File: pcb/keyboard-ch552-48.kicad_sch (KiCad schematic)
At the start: 112 parts, among them J1 USB_C_Receptacle_USB2.0, SW1 SW_SPST, SW2 SW_SPST, U1 CH552T

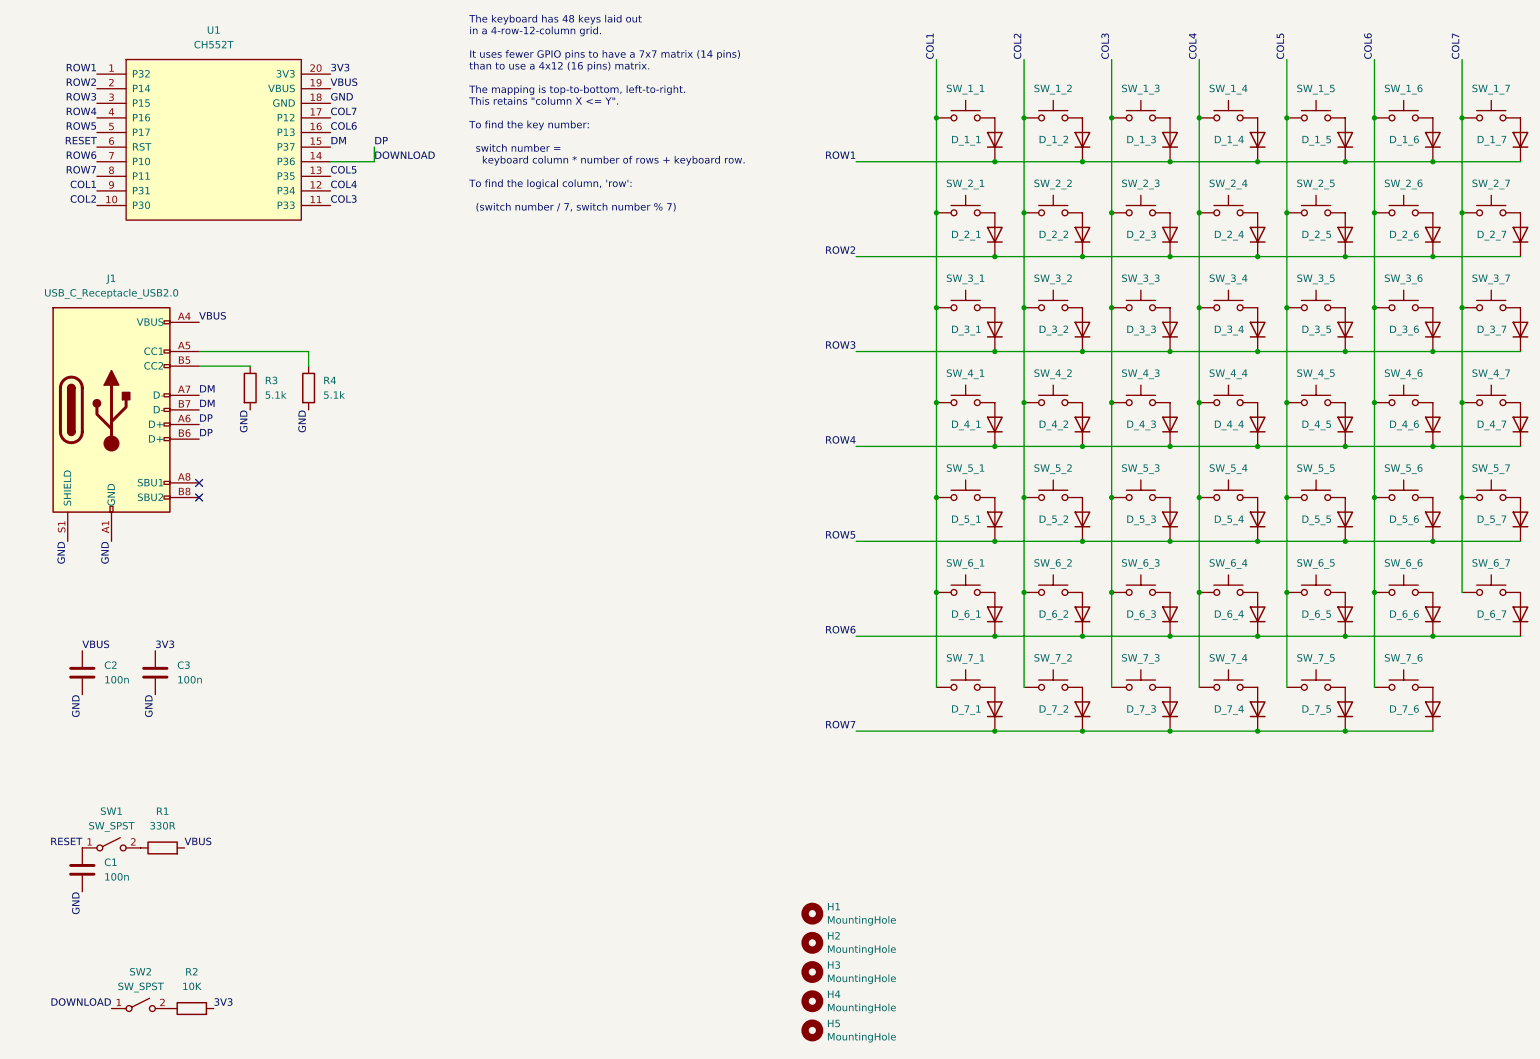
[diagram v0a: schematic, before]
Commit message: pcb: break out SPI pins for ISP flash on CH552-48
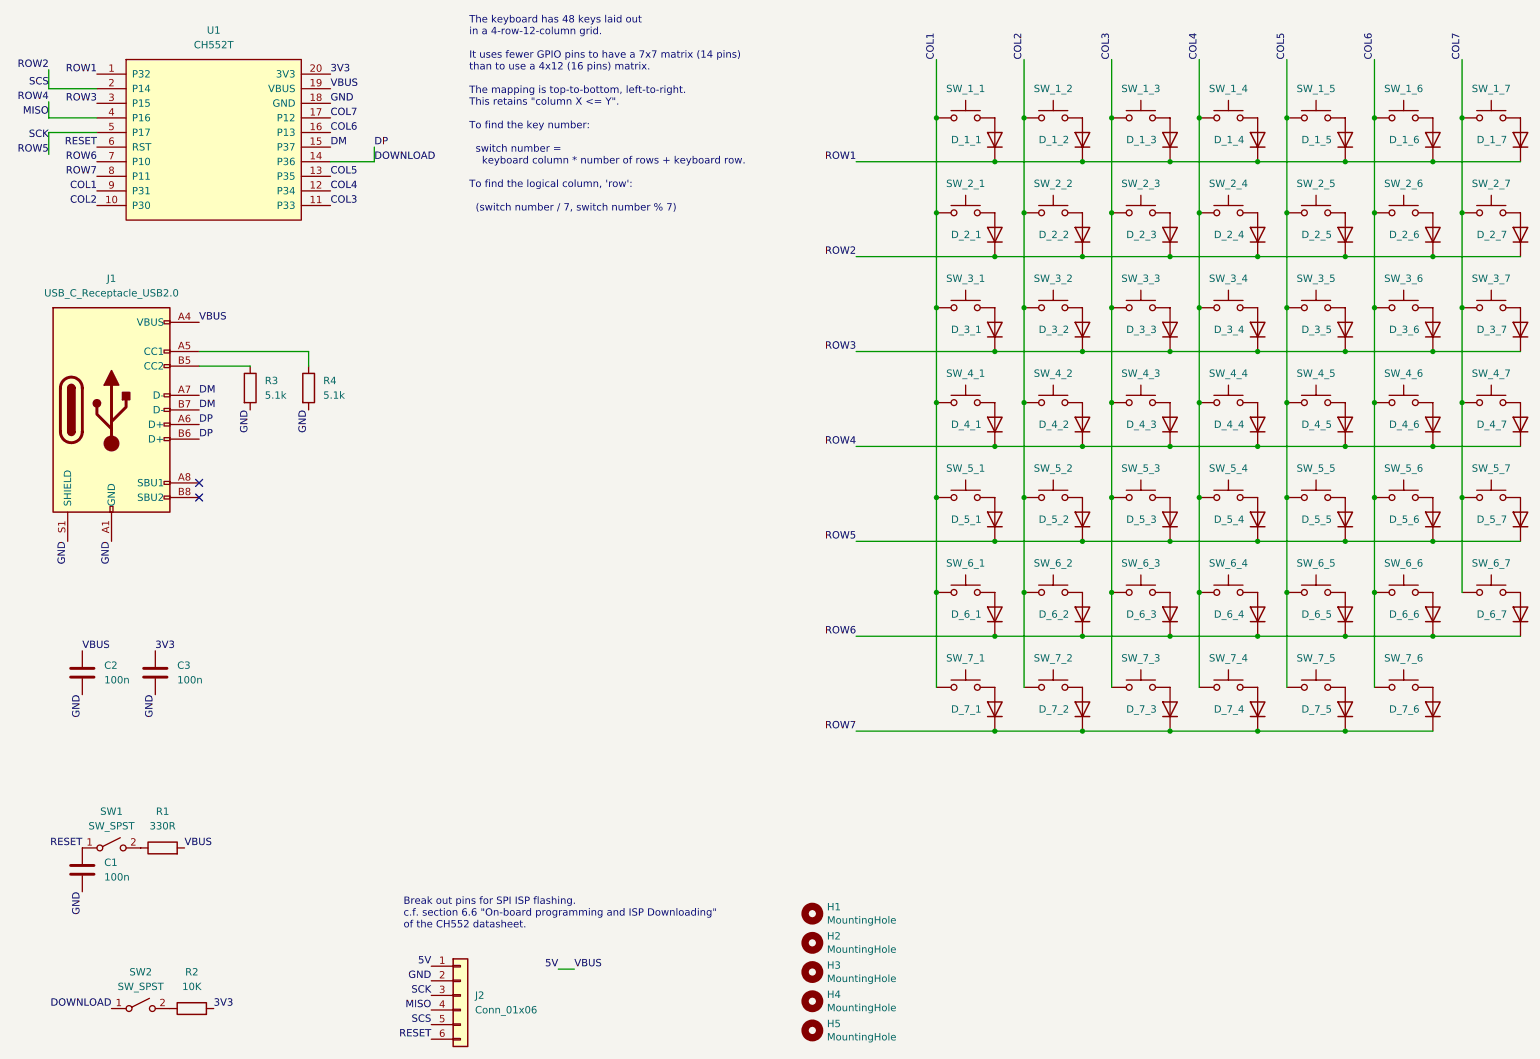
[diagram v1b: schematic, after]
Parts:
- added J2: Conn_01x06, symbol Connector_Generic:Conn_01x06
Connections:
- net GND: now also J2.2 (Pin_2)
- net RESET: now also J2.6 (Pin_6)
- net ROW2: now also J2.5 (Pin_5)
- net ROW5: now also J2.3 (Pin_3)
- net ROW4 renamed MISO
- net MISO: now also J2.4 (Pin_4)
- net VBUS renamed 5V
- net 5V: now also J2.1 (Pin_1)
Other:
- note added: "Break out pins for SPI ISP flashing. c.f. section 6.6 "On-board programming and ISP Downloading" of the CH552 datasheet."
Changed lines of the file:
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@@
   (title_block
     (title "CH552-48")
-    (date "2023-11-10")
-    (rev "rev2023.1")
+    (date "2024-01-03")
+    (rev "rev2024.1-pre")
     (company "Richard Goulter (rgoulter)")
     (comment 1 "48-key on 7x7 logical grid.")
@@
     (stroke (width 0) (type default))
   )
+  (wire (pts (xy 112.014 179.832) (xy 114.808 179.832))
+    (stroke (width 0) (type default))
+  )
   (wire (pts (xy 187.96 138.43) (xy 163.83 138.43))
     (stroke (width 0) (type default))
@@
     (stroke (width 0) (type default))
   )
+  (wire (pts (xy 23.368 28.956) (xy 23.368 31.75))
+    (stroke (width 0) (type default))
+  )
   (wire (pts (xy 254 97.79) (xy 254 114.3))
     (stroke (width 0) (type default))
@@
     (stroke (width 0) (type default))
   )
+  (wire (pts (xy 23.368 26.67) (xy 31.75 26.67))
+    (stroke (width 0) (type default))
+  )
   (wire (pts (xy 233.68 88.9) (xy 248.92 88.9))
     (stroke (width 0) (type default))
@@
     (stroke (width 0) (type default))
   )
+  (wire (pts (xy 23.368 31.75) (xy 31.75 31.75))
+    (stroke (width 0) (type default))
+  )
   (wire (pts (xy 223.52 114.3) (xy 223.52 130.81))
     (stroke (width 0) (type default))
@@
     (stroke (width 0) (type default))
   )
+  (wire (pts (xy 23.368 38.1) (xy 23.368 34.29))
+    (stroke (width 0) (type default))
+  )
   (wire (pts (xy 269.24 97.79) (xy 269.24 114.3))
     (stroke (width 0) (type default))
@@
     (stroke (width 0) (type default))
   )
+  (wire (pts (xy 23.368 23.368) (xy 23.368 26.67))
+    (stroke (width 0) (type default))
+  )
   (wire (pts (xy 254 31.75) (xy 254 48.26))
     (stroke (width 0) (type default))
@@
   )
   (wire (pts (xy 177.8 81.28) (xy 177.8 97.79))
+    (stroke (width 0) (type default))
+  )
+  (wire (pts (xy 23.368 34.29) (xy 31.75 34.29))
     (stroke (width 0) (type default))
   )
@@
     (effects (font (size 1.27 1.27)) (justify left bottom))
   )
+  (text "Break out pins for SPI ISP flashing.\nc.f. section 6.6 \"On-board programming and ISP Downloading\"\nof the CH552 datasheet."
+    (at 85.09 172.974 0)
+    (effects (font (size 1.27 1.27)) (justify left bottom))
+  )
+  (label "SCK" (at 23.368 35.56 180) (fields_autoplaced)
+    (effects (font (size 1.27 1.27)) (justify right bottom))
+  )
   (label "3V3" (at 72.39 24.13 0) (fields_autoplaced)
     (effects (font (size 1.27 1.27)) (justify left bottom))
@@
     (effects (font (size 1.27 1.27)) (justify left bottom))
   )
+  (label "5V" (at 89.916 179.324 180) (fields_autoplaced)
+    (effects (font (size 1.27 1.27)) (justify right bottom))
+  )
+  (label "SCK" (at 89.916 184.404 180) (fields_autoplaced)
+    (effects (font (size 1.27 1.27)) (justify right bottom))
+  )
   (label "COL4" (at 72.39 44.45 0) (fields_autoplaced)
     (effects (font (size 1.27 1.27)) (justify left bottom))
@@
     (effects (font (size 1.27 1.27)) (justify right bottom))
   )
+  (label "RESET" (at 89.916 192.024 180) (fields_autoplaced)
+    (effects (font (size 1.27 1.27)) (justify right bottom))
+  )
   (label "ROW4" (at 163.83 88.9 180) (fields_autoplaced)
     (effects (font (size 1.27 1.27)) (justify right bottom))
@@
     (effects (font (size 1.27 1.27)) (justify left bottom))
   )
+  (label "SCS" (at 89.916 189.484 180) (fields_autoplaced)
+    (effects (font (size 1.27 1.27)) (justify right bottom))
+  )
   (label "3V3" (at 41.91 124.46 0) (fields_autoplaced)
     (effects (font (size 1.27 1.27)) (justify left bottom))
   )
+  (label "SCS" (at 23.368 26.416 180) (fields_autoplaced)
+    (effects (font (size 1.27 1.27)) (justify right bottom))
+  )
   (label "DM" (at 49.53 82.55 0) (fields_autoplaced)
     (effects (font (size 1.27 1.27)) (justify left bottom))
@@
     (effects (font (size 1.27 1.27)) (justify right bottom))
   )
+  (label "VBUS" (at 114.808 179.832 0) (fields_autoplaced)
+    (effects (font (size 1.27 1.27)) (justify left bottom))
+  )
   (label "COL3" (at 208.28 21.59 90) (fields_autoplaced)
     (effects (font (size 1.27 1.27)) (justify left bottom))
   )
+  (label "5V" (at 112.014 179.832 180) (fields_autoplaced)
+    (effects (font (size 1.27 1.27)) (justify right bottom))
+  )
   (label "ROW5" (at 163.83 105.41 180) (fields_autoplaced)
     (effects (font (size 1.27 1.27)) (justify right bottom))
@@
     (effects (font (size 1.27 1.27)) (justify right bottom))
   )
-  (label "ROW4" (at 31.75 31.75 180) (fields_autoplaced)
+  (label "ROW4" (at 23.368 28.956 180) (fields_autoplaced)
+    (effects (font (size 1.27 1.27)) (justify right bottom))
+  )
+  (label "GND" (at 89.916 181.864 180) (fields_autoplaced)
     (effects (font (size 1.27 1.27)) (justify right bottom))
   )
@@
     (effects (font (size 1.27 1.27)) (justify right bottom))
   )
+  (label "MISO" (at 89.916 186.944 180) (fields_autoplaced)
+    (effects (font (size 1.27 1.27)) (justify right bottom))
+  )
   (label "ROW3" (at 163.83 72.39 180) (fields_autoplaced)
     (effects (font (size 1.27 1.27)) (justify right bottom))
@@
     (effects (font (size 1.27 1.27)) (justify right bottom))
   )
-  (label "ROW5" (at 31.75 34.29 180) (fields_autoplaced)
+  (label "ROW5" (at 23.368 38.1 180) (fields_autoplaced)
     (effects (font (size 1.27 1.27)) (justify right bottom))
   )
@@
     (effects (font (size 1.27 1.27)) (justify left bottom))
   )
-  (label "ROW2" (at 31.75 26.67 180) (fields_autoplaced)
+  (label "ROW2" (at 23.368 23.368 180) (fields_autoplaced)
     (effects (font (size 1.27 1.27)) (justify right bottom))
   )
   (label "DM" (at 49.53 80.01 0) (fields_autoplaced)
     (effects (font (size 1.27 1.27)) (justify left bottom))
+  )
+  (label "MISO" (at 23.368 31.496 180) (fields_autoplaced)
+    (effects (font (size 1.27 1.27)) (justify right bottom))
   )
   (label "VBUS" (at 72.39 26.67 0) (fields_autoplaced)
@@
         )
       )
+    )
+  )
+  (symbol (lib_id "Connector_Generic:Conn_01x06") (at 94.996 184.404 0) (unit 1)
+    (in_bom yes) (on_board yes) (dnp no) (fields_autoplaced)
+    (property "Reference" "J2" (at 97.536 184.404 0)
+      (effects (font (size 1.27 1.27)) (justify left))
+    )
+    (property "Value" "Conn_01x06" (at 97.536 186.944 0)
+      (effects (font (size 1.27 1.27)) (justify left))
+    )
+    (property "Footprint" "" (at 94.996 184.404 0)
+      (effects (font (size 1.27 1.27)) hide)
+    )
+    (property "Datasheet" "~" (at 94.996 184.404 0)
+      (effects (font (size 1.27 1.27)) hide)
+    )
+    (pin "1")
+    (pin "2")
+    (pin "3")
+    (pin "4")
+    (pin "5")
+    (pin "6")
+    (instances
+      (project "keyboard-ch552-48"
+        (path "/491af640-c615-48ab-84d8-9b166bc1ab37"
+          (reference "J2") (unit 1)
+        )
+      )
